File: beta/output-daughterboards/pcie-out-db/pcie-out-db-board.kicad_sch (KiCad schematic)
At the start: 7 parts, among them J1 PCIE8 OUT FIELD, J10 TE 63951-1, J11 TE 63951-1, J12 TE 63951-1, J13 TE 63951-1, J14 TE 63951-1, J15 TE 63951-1

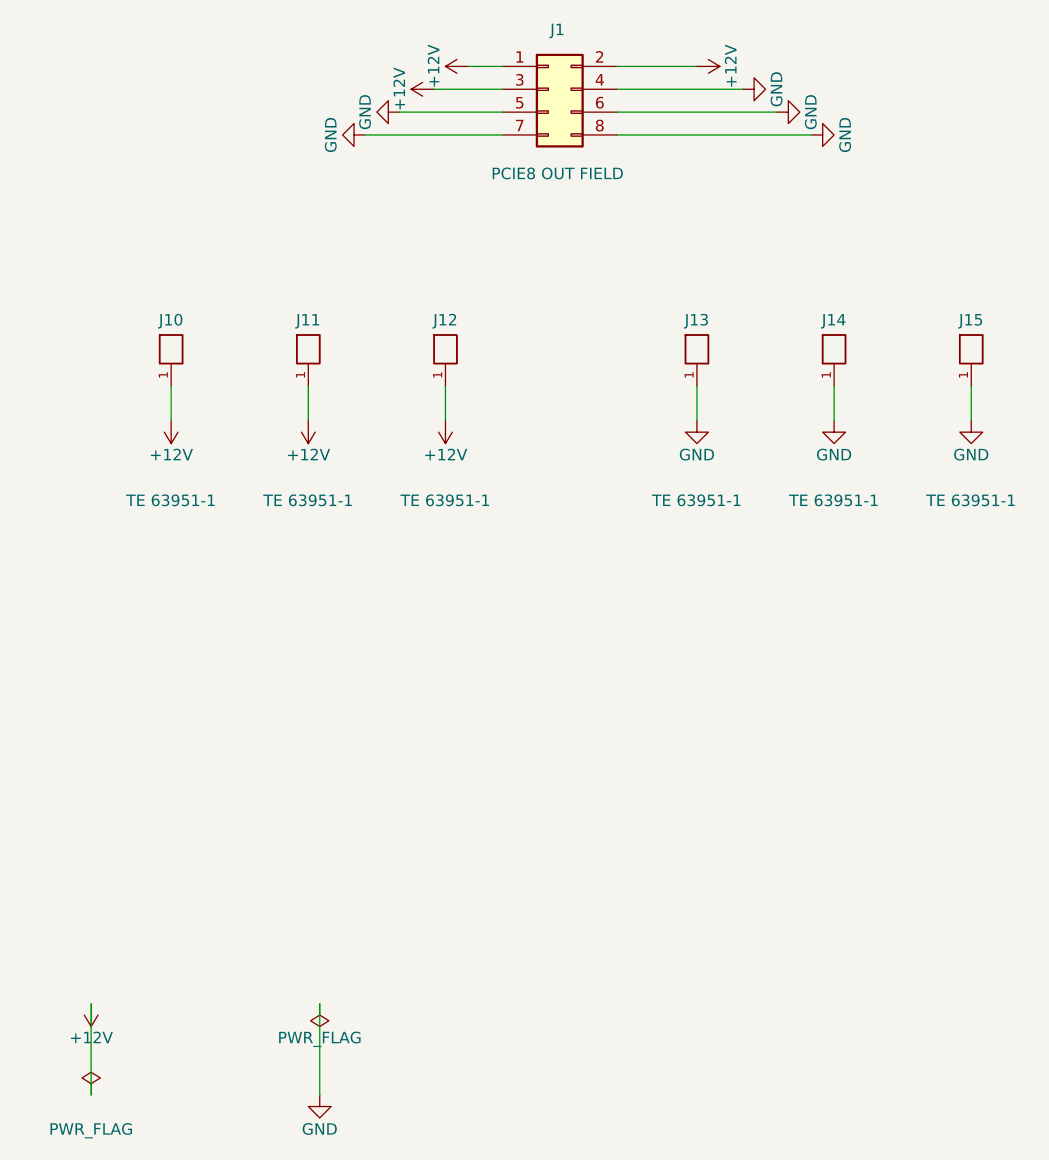
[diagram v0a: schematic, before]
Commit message: pipeline: integrate route-aware physical design flow
Generalize critical-first placement and routing, future-congestion and power-authority planning, route provenance, process watchdogs, fab/thermal validation, dashboard review, and XFCN integration. Add the supporting board contracts, component libraries, documentation, and regression coverage.
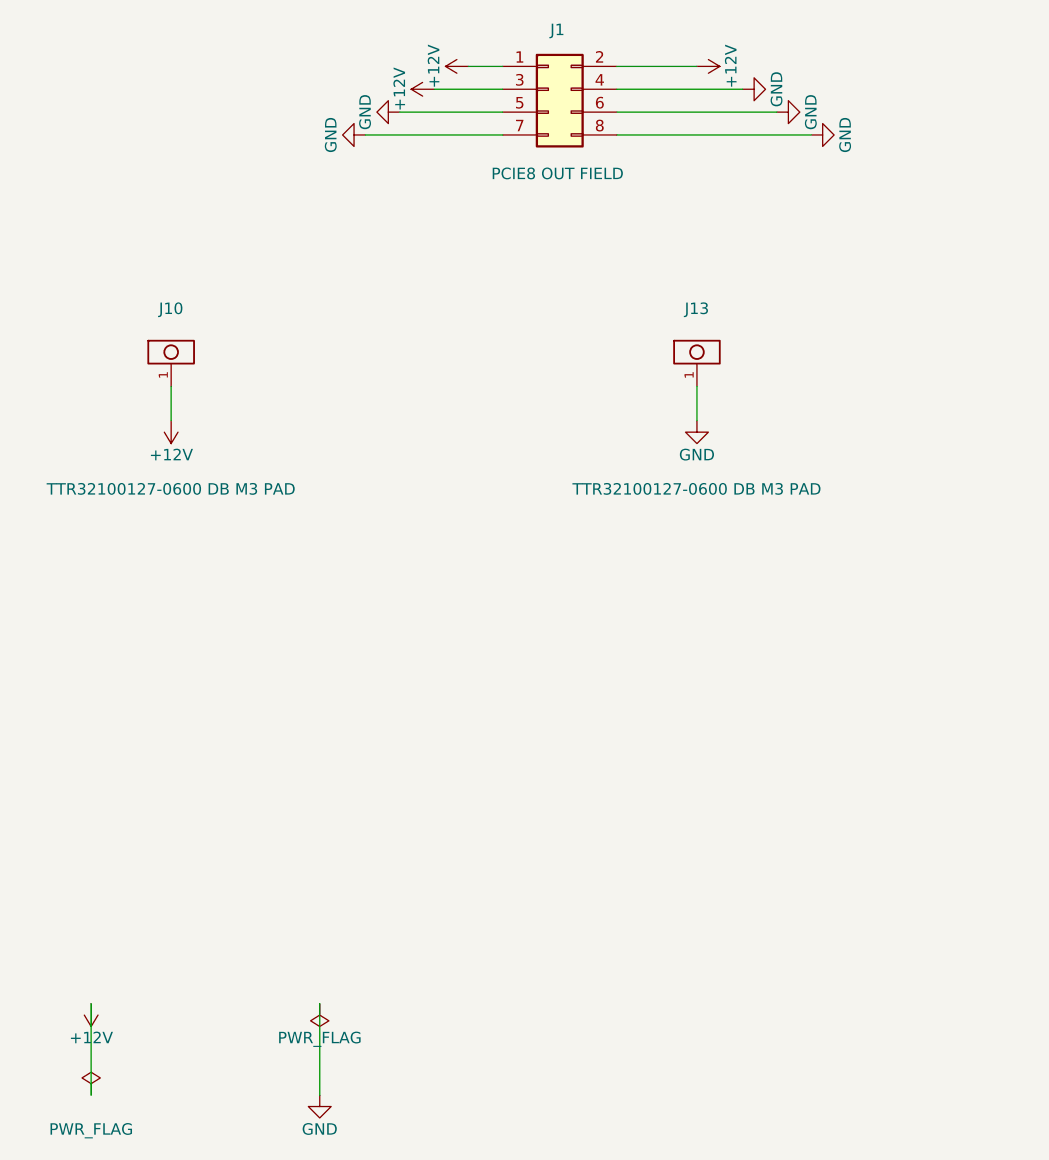
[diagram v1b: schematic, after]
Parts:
- removed J11, J12, J14, J15: TE 63951-1, cec-Connector_Blade:TE_63951-1_FASTON_Tab_250x032_RA_THT, symbol cec-vendor:TE_63951-1_FASTON_Tab
- J10, J13: value TE 63951-1 -> TTR32100127-0600 DB M3 PAD; footprint cec-Connector_Blade:TE_63951-1_FASTON_Tab_250x032_RA_THT -> cec-Connector_Screw:XFCN_TTR32100127-0600_Daughterboard_BoltPad_M3_PROVISIONAL; symbol cec-vendor:TE_63951-1_FASTON_Tab -> cec-Connector_Screw:XFCN_TTR32100127-0600_DB_BoltPad; Integration Note (none) -> Prototype XFCN interface; TE blade architecture remains the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; LCSC C591344 -> (none); MPN 63951-1 -> (none); Manufacturer TE Connectivity -> (none); Source Drawing (none) -> lib/datasheets/XFCN_TTR32100127-0600_C45384691.pdf; now left out of the parts list
